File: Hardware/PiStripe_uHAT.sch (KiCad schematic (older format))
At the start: 39 parts, among them J1 +12V, J2 LEDs, J3 IRRX, J4 RPi_GPIO, Q1 DMG2305UX-13, Q2 IRF8721PBF-1, Q3 IRF8721PBF-1, Q4 IRF8721PBF-1, U1 TPS54202, U2 DMMT5401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

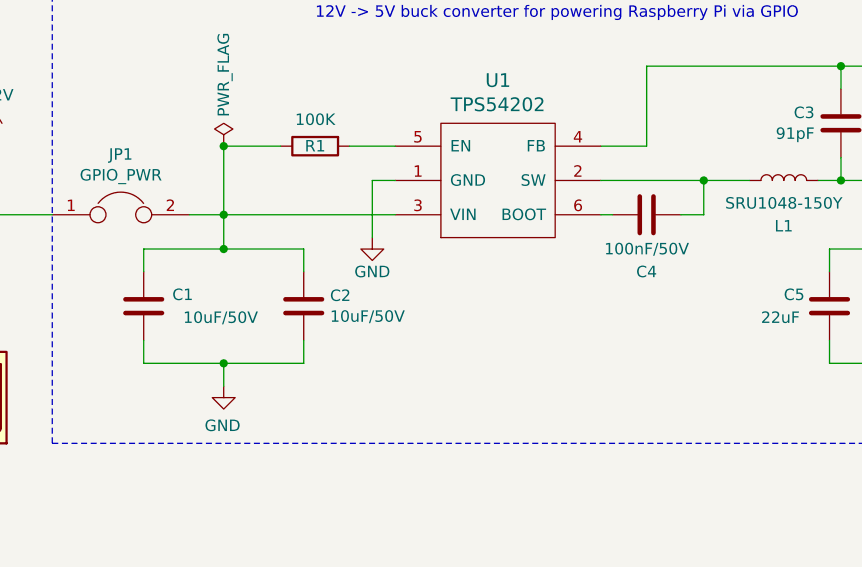
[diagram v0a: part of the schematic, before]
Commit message: Use 25V instead of 50V for C1, C2, C4
Should be totally sufficient and is available in 0805 form factor.
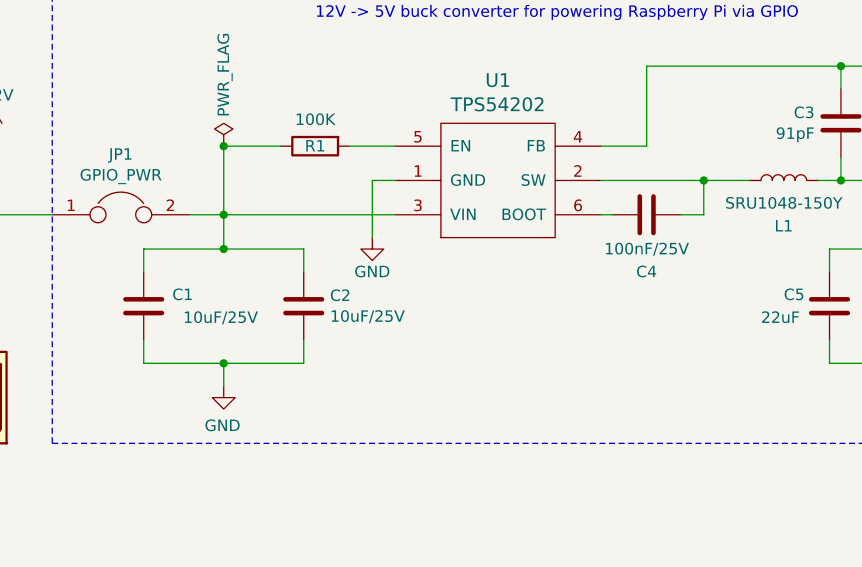
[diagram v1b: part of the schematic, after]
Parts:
- C1, C2: value 10uF/50V -> 10uF/25V
- C4: value 100nF/50V -> 100nF/25V
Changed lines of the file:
@@
 P 1950 6150
 F 0 "C1" H 1825 6200 50  0000 R CNN
-F 1 "10uF/50V" H 1450 6100 50  0000 L CNN
+F 1 "10uF/25V" H 1450 6100 50  0000 L CNN
 F 2 "Capacitor_SMD:C_0805_2012Metric_Pad1.15x1.40mm_HandSolder" H 1988 6000 50  0001 C CNN
 F 3 "~" H 1950 6150 50  0001 C CNN
@@
 P 4150 5750
 F 0 "C4" V 4400 5750 50  0000 C CNN
-F 1 "100nF/50V" V 4300 5750 50  0000 C CNN
+F 1 "100nF/25V" V 4300 5750 50  0000 C CNN
 F 2 "Capacitor_SMD:C_0805_2012Metric_Pad1.15x1.40mm_HandSolder" H 4188 5600 50  0001 C CNN
 F 3 "~" H 4150 5750 50  0001 C CNN
@@
 P 2650 6150
 F 0 "C2" H 2765 6196 50  0000 L CNN
-F 1 "10uF/50V" H 2765 6105 50  0000 L CNN
+F 1 "10uF/25V" H 2765 6105 50  0000 L CNN
 F 2 "Capacitor_SMD:C_0805_2012Metric_Pad1.15x1.40mm_HandSolder" H 2688 6000 50  0001 C CNN
 F 3 "~" H 2650 6150 50  0001 C CNN

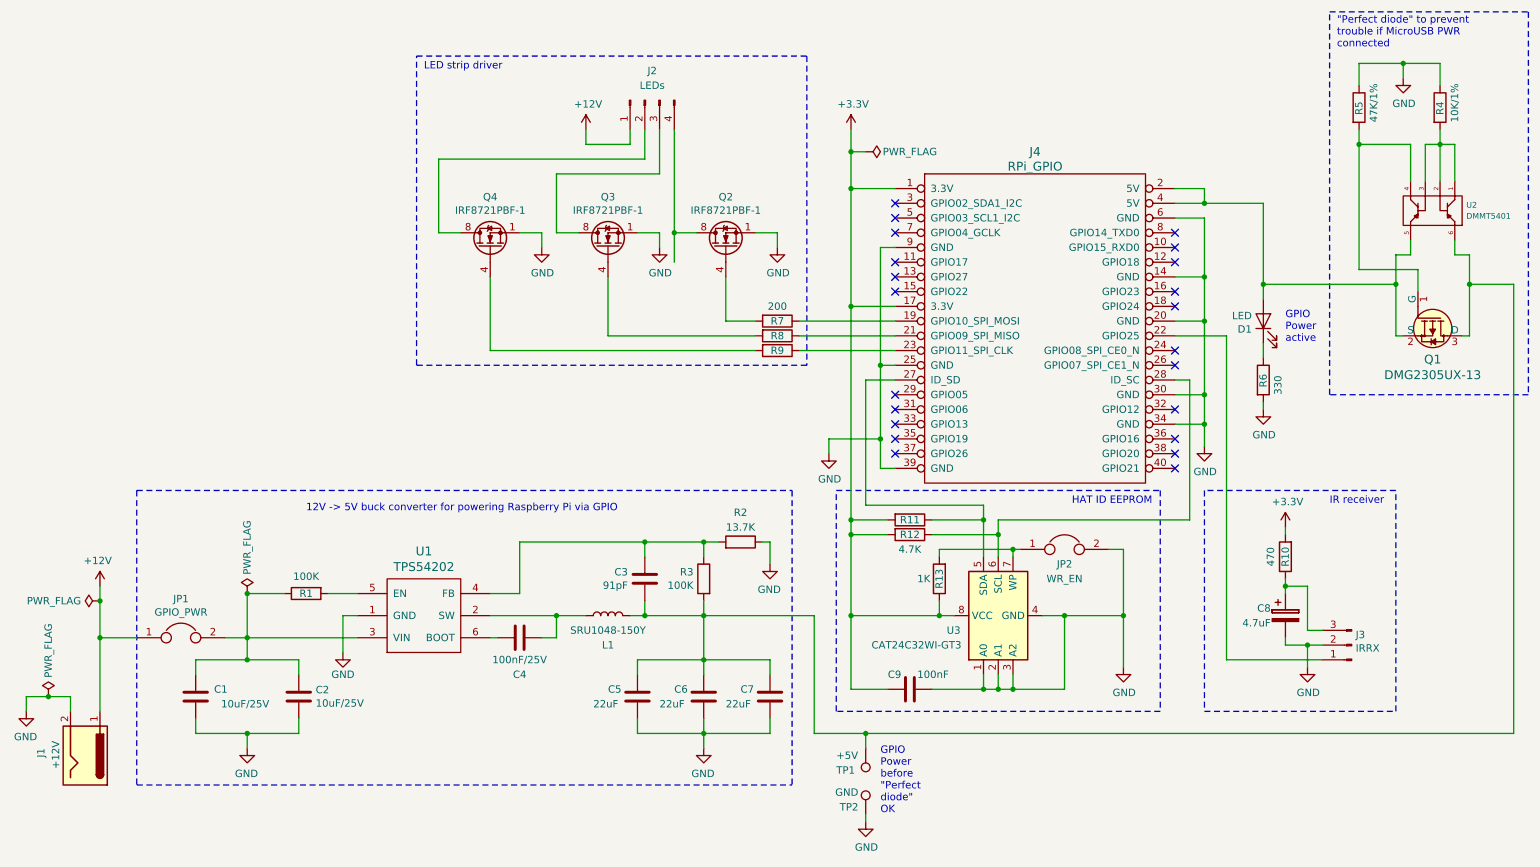
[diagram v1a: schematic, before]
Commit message: v0.6: Pulldowns for GPIO 09-11, reroute IRRX DATA, correct footprints etc.
- Added pulldown resistors on GPIO 09-11, the gate lines of the IRF8721PBFs
  to ensure an undefined state at powerup doesn't cause the MOSFETs to
  operate and make the LEDs flicker.
- Named nets in schematic for easier tracing in the PCB design.
- Rerouted IRRX DATA line on top side to avoid long GND-dividing trace on
  bottom side.
- Corrected parts and footprints for JP1 and JP2 to 2,54mm instead of
  1,27mm since these are supposed to be opened or closed via jumpers.
- Corrected part and footprint for J4 to a pin socket instead of a pin
  header since the PCB is supposed to be stacked on top of the Raspberry
  Pi. If you want to stack other uHATs on top of the PiStripe HAT, you
  can alternatively use a stacking header such as Adafruit's 1979, the
  pin holes are the same.
- Added more Vias to the ground plane on the bottom side.
- Added text on top side indicating Pin 1 of parts and LED orientation.
- Removed orphaned trace hidden underneath mounting hole 1.

Thanks to @xor@chaos.social and @struppi@chaos.social for their design
review and advice!
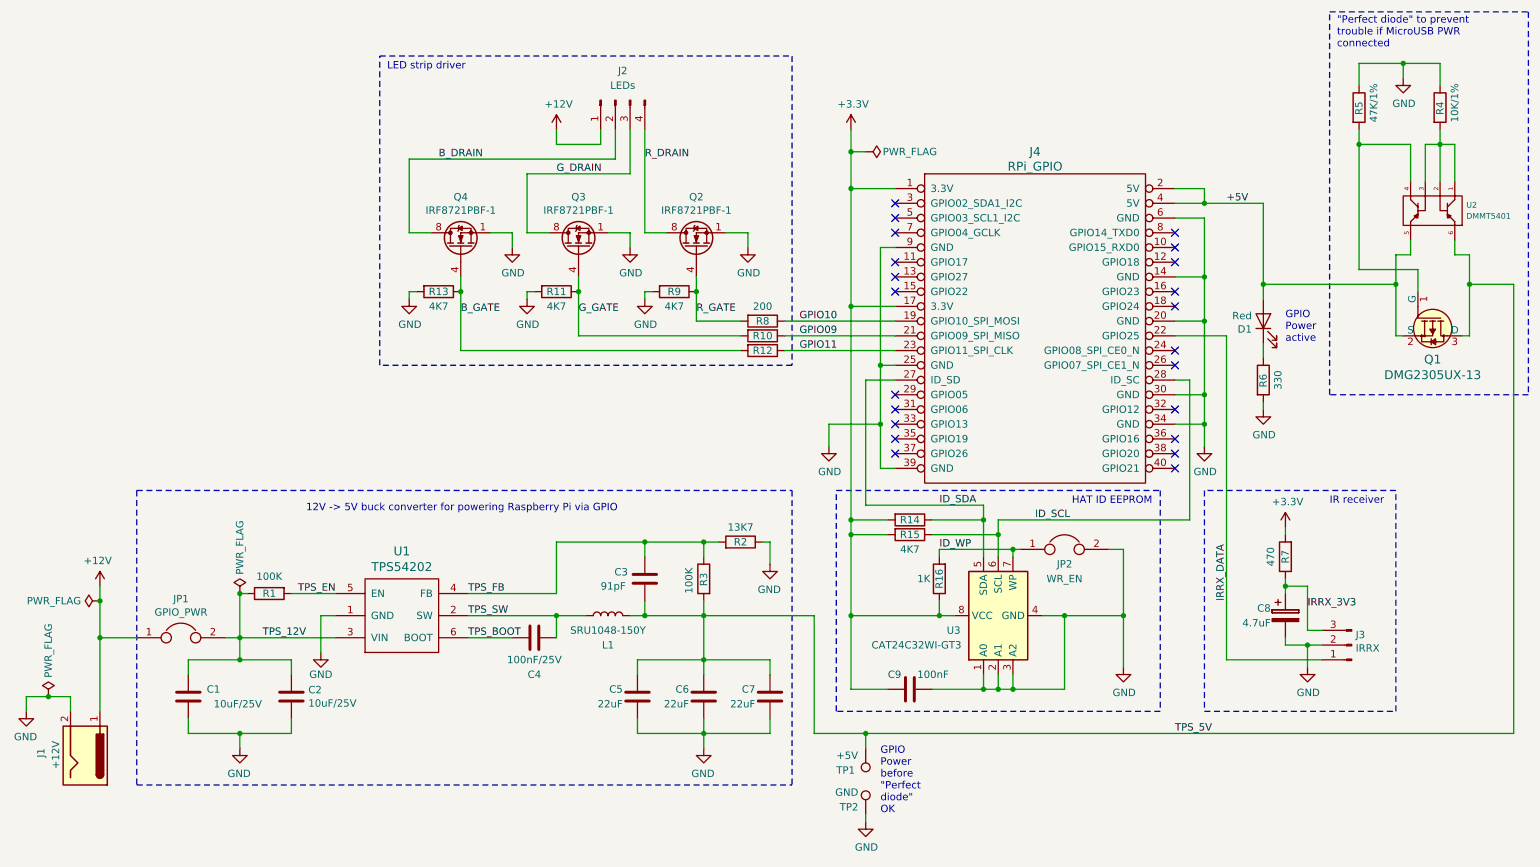
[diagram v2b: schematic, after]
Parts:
- added R11, R13, R9: 4K7, Resistor_SMD:R_0805_2012Metric_Pad1.15x1.40mm_HandSolder, symbol Device:R
- D1: value LED -> Red
- J4: footprint Connector_PinHeader_2.54mm:PinHeader_2x20_P2.54mm_Vertical -> Connector_PinSocket_2.54mm:PinSocket_2x20_P2.54mm_Vertical
- JP1, JP2: footprint Connector_PinHeader_1.27mm:PinHeader_1x02_P1.27mm_Vertical -> Connector_PinHeader_2.54mm:PinHeader_1x02_P2.54mm_Vertical
- R14: renamed from R11; value 4.7K -> 4K7
- R15: renamed from R12; value 4.7K -> 4K7
- R2: value 13.7K -> 13K7
- renumbered R8 to R10, R9 to R12, R13 to R16, R10 to R7, R7 to R8
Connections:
- net GND: now also R11.2, R13.2, R9.2
- net GPIO10: now reaches J4.19 (GPIO10_SPI_MOSI), R8.1
- net +5V: now reaches D1.2 (A), J4.2 (5V), J4.4 (5V), Q1.2 (S), U2.5
- net GPIO09: now reaches J4.21 (GPIO09_SPI_MISO), R10.1
- net IRRX_DATA: now reaches J3.1 (Pin_1), J4.22 (GPIO25)
- net GPIO11: now reaches J4.23 (GPIO11_SPI_CLK), R12.1
- net ID_SDA: now reaches J4.27 (ID_SD), R14.1, U3.5 (SDA)
- net ID_SCL: now reaches J4.28 (ID_SC), R15.1, U3.6 (SCL)
- net B_DRAIN: now reaches J2.2 (Pin_2), Q4.5 (D), Q4.6 (D), Q4.7 (D), Q4.8 (D)
- net G_DRAIN: now reaches J2.3 (Pin_3), Q3.5 (D), Q3.6 (D), Q3.7 (D), Q3.8 (D)
- net R_DRAIN: now reaches J2.4 (Pin_4), Q2.5 (D), Q2.6 (D), Q2.7 (D), Q2.8 (D)
- net B_GATE: now reaches Q4.4 (G), R12.2
- net B_GATE: now also R13.1
- net G_GATE: now reaches Q3.4 (G), R10.2
- net G_GATE: now also R11.1
- net R_GATE: now reaches Q2.4 (G), R8.2
- net R_GATE: now also R9.1
- net TPS_5V: now reaches C3.2, C5.1, C6.1, C7.1, L1.1, Q1.3 (D), R3.2, TP1.1, U2.6
- net TPS_SW: now reaches C4.2, L1.2, U1.2 (SW)
- net TPS_12V: now reaches C1.1, C2.1, JP1.2, R1.1, U1.3 (VIN)
- net TPS_FB: now reaches C3.1, R2.2, R3.1, U1.4 (FB)
- net TPS_EN: now reaches R1.2, U1.5 (EN)
- net TPS_BOOT: now reaches C4.1, U1.6 (BOOT)
- net ID_WP: now reaches JP2.1, R16.2, U3.7 (WP)
- net IRRX_3V3: now reaches C8.1, J3.3 (Pin_3), R7.1
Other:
- moved on the sheet: C1, C2, C4, J2, Q2, Q3, Q4, R1, R10, R12, R8, U1

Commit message: v0.7: Correct connections and footprints for J2 and J3
- Corrected J2 connections from R/G/B/+12V to B/R/G/+12V layout
  because that's what most LED strips actually use connector-wise.
- Flipped J3 connections, Pin 1/DATA is now left, so that you can
  solder in a TSOP4838 directly if you want to.
- Corrected footprints for J2 and J3 to 2.54mm pitch.
- This required moving J1 and the entire voltage regulator
  section a bit to the left, rotating U3 and rearranging related
  parts as well as moving R7 and C8 for the TSOP.
- Changed JP2 to 1.27mm pitch again because there are actually
  1.27mm jumpers available, the space was needed and this jumper is
  less likely to be changed than JP1.
- Refer to CSV parts list instead of repeating its contents in README
  that easily gets outdated.
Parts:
- C9: value 100nF -> 100nF/25V
- J2: footprint Connector_PinHeader_1.27mm:PinHeader_1x04_P1.27mm_Horizontal -> Connector_PinSocket_2.54mm:PinSocket_1x04_P2.54mm_Horizontal
- J3: footprint Connector_PinHeader_1.27mm:PinHeader_1x03_P1.27mm_Horizontal -> pief:PinHeader_1x03_P2.54mm_Horizontal_Mirrored
- JP2: footprint Connector_PinHeader_2.54mm:PinHeader_1x02_P2.54mm_Vertical -> Connector_PinHeader_1.27mm:PinHeader_1x02_P1.27mm_Vertical
- R10, R12, R8: value 200 -> 220
- renumbered R9 to R13, R13 to R9
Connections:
- net +12V: now also J2.4 (Pin_4); no longer J2.1 (Pin_1)
- net B_DRAIN: now also J2.1 (Pin_1), Q2.5 (D), Q2.6 (D), Q2.7 (D), Q2.8 (D); no longer J2.2 (Pin_2), Q4.5 (D), Q4.6 (D), Q4.7 (D), Q4.8 (D)
- net B_GATE: now also Q2.4 (G), R8.2; no longer Q4.4 (G), R12.2
- net G_DRAIN: now also Q4.5 (D), Q4.6 (D), Q4.7 (D), Q4.8 (D); no longer Q3.5 (D), Q3.6 (D), Q3.7 (D), Q3.8 (D)
- net G_GATE: now also Q4.4 (G), R12.2, R13.1; no longer Q3.4 (G), R10.2, R11.1
- net R_DRAIN: now also J2.2 (Pin_2), Q3.5 (D), Q3.6 (D), Q3.7 (D), Q3.8 (D); no longer J2.4 (Pin_4), Q2.5 (D), Q2.6 (D), Q2.7 (D), Q2.8 (D)
- net R_GATE: now also Q3.4 (G), R10.2, R11.1; no longer Q2.4 (G), R13.1, R8.2
- net DMMT_BC12: now reaches R4.2, U2.1, U2.2, U2.3
- net DMMT_BC34: now reaches Q1.1 (G), R5.2, U2.4
- net LED_+5V: now reaches D1.1 (K), R6.1
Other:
- moved on the sheet: C9, J2, R11, R13, R6, R9
